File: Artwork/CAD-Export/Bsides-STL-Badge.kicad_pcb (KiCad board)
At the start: 2 copper layers, 93.5 x 137.1 mm, 7 parts

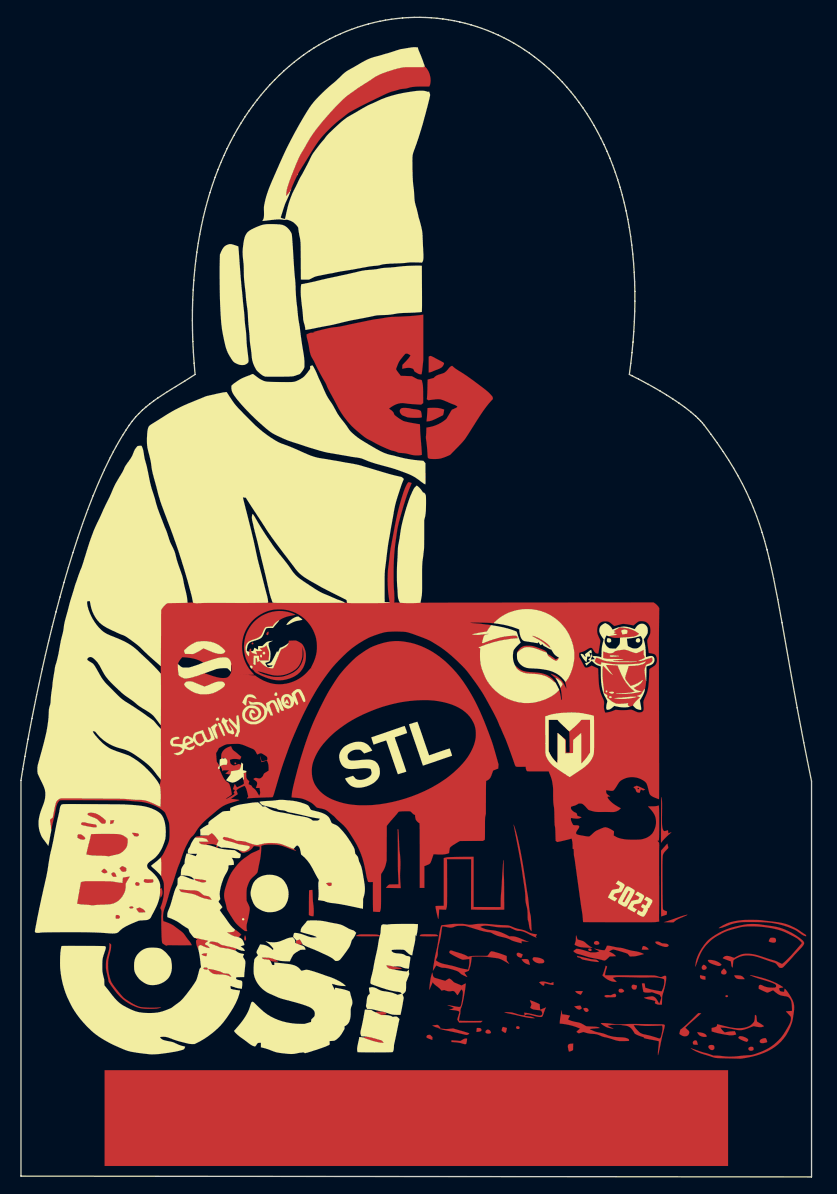
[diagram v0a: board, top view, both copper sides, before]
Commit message: Updated Edge Cut
Edge cut in artwork and exported to CAD
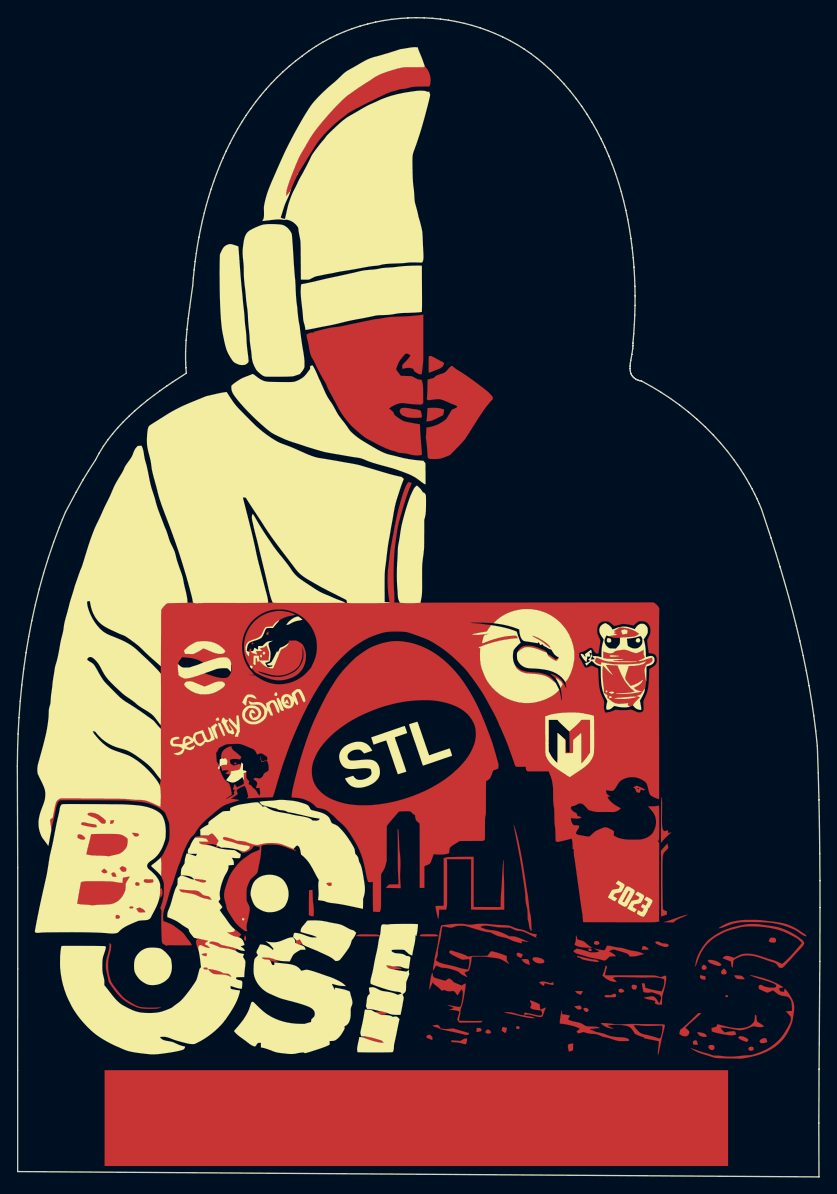
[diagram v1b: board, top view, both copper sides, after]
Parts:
- removed the G*** at (0.00, 0.00) (x7)
- added G*** (x7): LOGO, LOGO, F.Cu at (0.00, 0.00)
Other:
- board size 93.5 x 137.1 mm -> 94.9 x 137 mm

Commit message: laying out with no elect
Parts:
- removed the G*** at (0.00, 0.00) (x7)
- added G***: NG_BSilk_B.Cu, BadgePiratesLogos:NG_B.Cu, F.Cu at (158.7, 155.4)
- added G***: fg, BadgePiratesLogos:FG_B.Cu, F.Cu at (109.4, 154.5)
- added G*** (x7): LOGO, LOGO, F.Cu at (128.8, 94.6)
- added G***: BP Logo, BadgePiratesLogos:BPSkull_Distressed_B.SILK, F.Cu at (133.5, 87.7)
- added G***: LOGO, BadgePiratesLogos:BadgePiratesURL_B.SLK, F.Cu at (135.0, 80.1)
- added REF**: 5.5mm, BadgePirates:Hole_5.5mm, F.Cu at (134.1, 28.5)
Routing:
- added copper zone on B.Cu, net (none)
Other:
- outline, holes or cut-outs redrawn
- net class Default removed
